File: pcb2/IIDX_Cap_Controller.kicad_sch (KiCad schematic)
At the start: 12 parts, among them J1 Conn_01x01, J10 Conn_01x12_Pin, J11 Conn_01x07_Pin, J2 Conn_01x01, J3 Conn_01x01, J4 Conn_01x01, J5 Conn_01x01, J6 Conn_01x01, J7 Conn_01x01, J8 Conn_01x07_Pin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

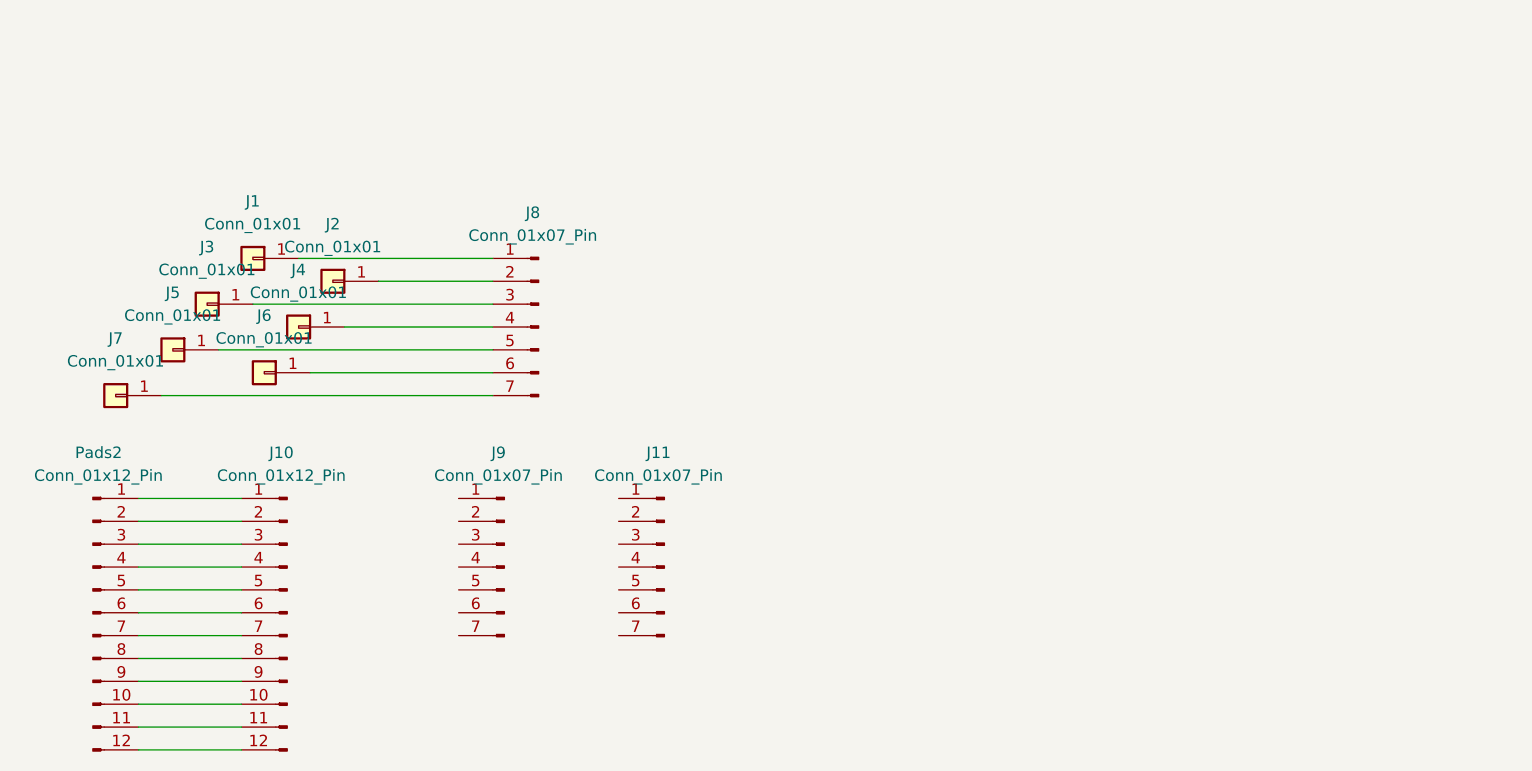
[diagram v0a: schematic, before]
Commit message: feat: layout & routing with pico onboard
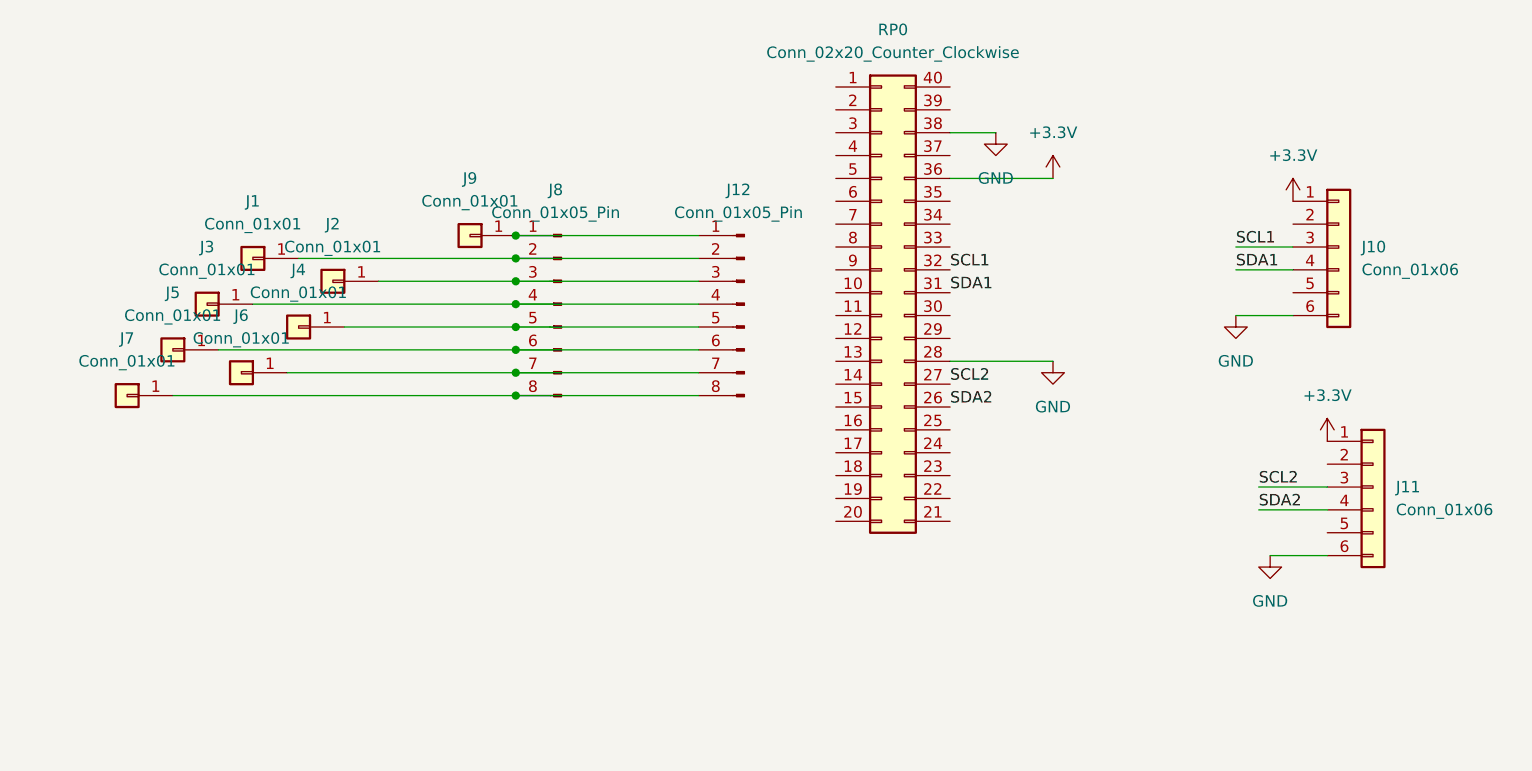
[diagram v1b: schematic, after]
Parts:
- removed J10, Pads2: Conn_01x12_Pin, symbol Connector:Conn_01x12_Pin
- removed J11, J8, J9: Conn_01x07_Pin, Connector_PinHeader_2.54mm:PinHeader_1x07_P2.54mm_Vertical, symbol Connector:Conn_01x07_Pin
- added J10: Conn_01x06, Connector_PinHeader_2.54mm:PinHeader_1x06_P2.54mm_Vertical, symbol Connector_Generic:Conn_01x06
- added J11: Conn_01x06, symbol Connector_Generic:Conn_01x06
- added J12: Conn_01x05_Pin, Connector_PinHeader_2.54mm:PinHeader_1x08_P2.54mm_Vertical_SMD_Pin1Left, symbol Connector:Conn_01x08_Pin
- added J8: Conn_01x05_Pin, Connector_PinHeader_2.54mm:PinHeader_1x08_P2.54mm_Vertical, symbol Connector:Conn_01x08_Pin
- added J9: Conn_01x01, clipboard:4807e8d7-bff8-4c85-8422-397af0b06065, symbol Connector_Generic:Conn_01x01
- added RP0: Conn_02x20_Counter_Clockwise, symbol Connector_Generic:Conn_02x20_Counter_Clockwise
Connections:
- net at J5.1 (Pin_1): now also J12.6 (Pin_6), J8.6 (Pin_6)
- net at J1.1 (Pin_1): now also J12.2 (Pin_2), J8.2 (Pin_2)
- net at J7.1 (Pin_1): now also J12.8 (Pin_8), J8.8 (Pin_8)
- net at J3.1 (Pin_1): now also J12.4 (Pin_4), J8.4 (Pin_4)
- net at J4.1 (Pin_1): now also J12.5 (Pin_5), J8.5 (Pin_5)
- net at J2.1 (Pin_1): now also J12.3 (Pin_3), J8.3 (Pin_3)
- net at J6.1 (Pin_1): now also J12.7 (Pin_7), J8.7 (Pin_7)
- new net: J12.1 (Pin_1), J8.1 (Pin_1), J9.1 (Pin_1)
- new net +3.3V: J10.1 (Pin_1), J11.1 (Pin_1), RP0.36 (Pin_36)
- new net GND: J10.6 (Pin_6), J11.6 (Pin_6), RP0.28 (Pin_28), RP0.38 (Pin_38)
- new net SCL1: J10.3 (Pin_3), RP0.32 (Pin_32)
- new net SCL2: J11.3 (Pin_3), RP0.27 (Pin_27)
- new net SDA1: J10.4 (Pin_4), RP0.31 (Pin_31)
- new net SDA2: J11.4 (Pin_4), RP0.26 (Pin_26)
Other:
- moved on the sheet: J6, J7
